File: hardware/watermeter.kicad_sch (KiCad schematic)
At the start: 23 parts, among them J1 flow_meter, J2 t_in, J3 t_out, J4 USB-TYPE-C-31-M-12, SW1 Reboot, U2 ESP32-C6-MINI-1, U3 USBLC6-2SC6

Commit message: Refactoring
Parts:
- removed J2: t_in, Connector_PinHeader_2.00mm:PinHeader_1x03_P2.00mm_Horizontal, symbol Connector_Generic:Conn_01x03
- removed J3: t_out, Connector_PinHeader_2.00mm:PinHeader_1x03_P2.00mm_Horizontal, symbol Connector_Generic:Conn_01x03
- removed J4: USB-TYPE-C-31-M-12, MyFootprints:USB-HRO_TYPE-C-31-M-12, symbol MyParts:USB-TYPE-C-31-M-12
- removed R1, R2: 3.3k, Resistor_SMD:R_0805_2012Metric, symbol Device:R
- removed R6, R7: 22R, Resistor_SMD:R_0805_2012Metric, symbol Device:R
- removed R8, R9: 5.1, Resistor_SMD:R_0805_2012Metric, symbol Device:R
- removed U3: USBLC6-2SC6, Package_TO_SOT_SMD:SOT-23-6, symbol Power_Protection:USBLC6-2SC6
- added J1: TC2030, Connector:Tag-Connect_TC2030-IDC-NL_2x03_P1.27mm_Vertical, symbol Connector:TC2030
- added J2: EXT, Connector_PinHeader_2.54mm:PinHeader_1x13_P2.54mm_Vertical, symbol Connector:Conn_01x13_Pin
- added J4: PT1000-1, Connector_Wire:SolderWire-0.1sqmm_1x02_P3.6mm_D0.4mm_OD1mm_Relief, symbol Connector:Conn_01x02_Pin
- added J5: PT1000-2, Connector_Wire:SolderWire-0.1sqmm_1x02_P3.6mm_D0.4mm_OD1mm_Relief, symbol Connector:Conn_01x02_Pin
- C1: DIGIKEY Part # (none) -> 1276-1076-1-ND; MP (none) -> CL05A105KP5NNNC
- C2: renamed from C9; DIGIKEY Part # (none) -> 1276-1193-1-ND; MP (none) -> CL10A226MQ8NRNC
- C3: renamed from C10; DIGIKEY Part # (none) -> 311-1701-1-ND; MP (none) -> CC0402KRX7R5BB104
- D1: renamed from D26; LCSC Part # (none) -> C2297
- D2: renamed from D1; LCSC Part # (none) -> C2293
- J3: renamed from J1; footprint Connector_PinHeader_2.00mm:PinHeader_1x03_P2.00mm_Horizontal -> Connector_Wire:SolderWire-0.1sqmm_1x03_P3.6mm_D0.4mm_OD1mm_Relief
- R1: renamed from R23; LCSC Part # C25804 -> C17414
- R2: renamed from R45; LCSC Part # (none) -> C17544
- R3: renamed from R5; LCSC Part # (none) -> C17480
- R6: renamed from R3; LCSC Part # (none) -> C17513
- R7: renamed from R4; LCSC Part # (none) -> C17604
- renumbered U2 to U1
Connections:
- net +3.3V: now also J2.1 (Pin_1)
- net +5V: now also J2.12 (Pin_12)
- net 5V_USB: now also J1.2
- net GND: now also J1.4, J2.13 (Pin_13)
- net at U1.10 (IO5): now also J2.7 (Pin_7)
- net at U1.12 (IO0): now also J2.2 (Pin_2)
- net at U1.13 (IO1): now also J2.3 (Pin_3)
- net at U1.15 (IO6): now also J2.8 (Pin_8)
- net at U1.16 (IO7): now also J2.9 (Pin_9)
- net at U1.22 (IO8): now also J2.10 (Pin_10)
- net at U1.23 (IO9): now also J2.11 (Pin_11)
- net RXD: now reaches U1.30 (RXD0)
- net RXD: now also J1.5
- net TXD: now reaches U1.31 (TXD0)
- net TXD: now also J1.3
- net at U1.5 (IO2): now also J2.4 (Pin_4)
- net at U1.6 (IO3): now also J2.5 (Pin_5)
- net at U1.9 (IO4): now also J2.6 (Pin_6)
- net USB_D_N: no longer names the net of U1.17 (IO12)
- net USB_D_P: no longer names the net of U1.18 (IO13)
- new net BOOT: J1.6
- new net EN: J1.1
- no-connect marks 18 -> 3
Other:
- moved on the sheet: J3, R6, R7, U1

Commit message: Schematics done
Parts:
- removed J1: TC2030, Connector:Tag-Connect_TC2030-IDC-NL_2x03_P1.27mm_Vertical, symbol Connector:TC2030
- removed J2: EXT, Connector_PinHeader_2.54mm:PinHeader_1x13_P2.54mm_Vertical, symbol Connector:Conn_01x13_Pin
- added C10, C11, C12, C13: 0.1uF, Capacitor_SMD:C_0402_1005Metric, symbol Device:C
- added D7, D8: 1N4148W, PCM_Diode_SMD_AKL:D_SOD-123, symbol PCM_Diode_AKL:1N4148W
- added J1: NTC1, Connector_Wire:SolderWire-0.1sqmm_1x02_P3.6mm_D0.4mm_OD1mm_Relief, symbol Connector:Conn_01x02_Pin
- added J10, J11: Screw_Terminal_01x03, symbol Connector:Screw_Terminal_01x03
- added J12: Screw, symbol Connector:Screw_Terminal_01x02
- added J13, J14: Conn_01x06_Shielded, symbol Connector:Conn_01x06_Pin
- added J2: DHT21, Connector_Wire:SolderWire-0.1sqmm_1x03_P3.6mm_D0.4mm_OD1mm_Relief, symbol Connector_Generic:Conn_01x03
- added J7: NTC3, Connector_Wire:SolderWire-0.1sqmm_1x02_P3.6mm_D0.4mm_OD1mm_Relief, symbol Connector:Conn_01x02_Pin
- added J8: NTC4, Connector_Wire:SolderWire-0.1sqmm_1x02_P3.6mm_D0.4mm_OD1mm_Relief, symbol Connector:Conn_01x02_Pin
- added J9: USB-TYPE-C-31-M-12, MyFootprints:USB-HRO_TYPE-C-31-M-12, symbol MyParts:USB-TYPE-C-31-M-12
- added K1, K2: SRD-05VDC-SL-C, Relay_THT:Relay_SPDT_SANYOU_SRD_Series_Form_C, symbol Relay:SANYOU_SRD_Form_C
- added OC1, OC2: TLP2361, PCM_Package_SO_AKL:SO-5_4.4x3.6mm_P1.27mm, symbol PCM_Optocoupler_Logic_AKL:TLP2361
- added Q1, Q2: NPN, symbol Simulation_SPICE:NPN
- added R10: 10K, Resistor_SMD:R_0805_2012Metric, symbol Device:R
- added R11, R12: 5.1, Resistor_SMD:R_0805_2012Metric, symbol Device:R
- added R13, R16: 22R, Resistor_SMD:R_0805_2012Metric, symbol Device:R
- added R17, R18, R4, R5, R8, R9: 4k7, symbol Device:R
- added R19: 1k, Resistor_SMD:R_0805_2012Metric, symbol Device:R
- added U2: USBLC6-2SC6, Package_TO_SOT_SMD:SOT-23-6, symbol Power_Protection:USBLC6-2SC6
- J4: value PT1000-1 -> NTC1
- J5: value PT1000-2 -> NTC2
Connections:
- net +3.3V: now also J14.1 (Pin_1), J2.1 (Pin_1), OC2.6 (VCC), R10.1, R18.1, R4.1, R5.1, R8.1, R9.1
- net +5V: now also D7.1 (K), D8.1 (K), J13.1 (Pin_1), K1.2, K2.2, OC1.6 (VCC), R17.1
- net 5V_USB: now also J9.A4_B9 (VBUS), J9.B4_A9 (VBUS), U2.5 (VBUS)
- net GND: now also J4.2 (Pin_2), J5.2 (Pin_2), C10.2, C11.2, C12.2, C13.2, J13.6 (Pin_6), J14.6 (Pin_6), J2.3 (Pin_3), J7.2 (Pin_2), J8.2 (Pin_2), J9.A1_B12 (GND), J9.B1_A12 (GND), OC1.3, OC2.4 (GND), Q1.3 (E), Q2.3 (E), R11.2, R12.2, U2.2 (GND)
- net IO1: now reaches J4.1 (Pin_1)
- net IO1: now also U1.13 (IO1), C10.1, R9.2
- net IO23: now reaches D1.2 (A), U1.29 (IO23)
- net IO7: now reaches R6.2, R7.1
- net IO7: now also U1.16 (IO7); no longer U1.27 (IO21)
- net IO22: now reaches D2.2 (A), U1.28 (IO22)
- net IO22: now also J14.5 (Pin_5)
- net IO3: now reaches J5.1 (Pin_1)
- net IO3: now also U1.6 (IO3), C11.1, R8.2
- net IO5: now reaches U1.10 (IO5)
- net IO5: now also C13.1, J8.1 (Pin_1), R4.2
- net IO0: now reaches U1.12 (IO0)
- net IO0: now also J13.2 (Pin_2)
- net IO6: now reaches U1.15 (IO6)
- net IO6: now also J2.2 (Pin_2), R10.2
- net USB_D_N: now reaches U1.17 (IO12)
- net USB_D_N: now also R13.2
- net USB_D_P: now reaches U1.18 (IO13)
- net USB_D_P: now also R16.2
- net IO14: now reaches U1.19 (IO14)
- net IO14: now also OC2.5, R18.2
- net IO15: now reaches U1.20 (IO15)
- net IO15: now also OC1.1
- net IO8: now reaches U1.22 (IO8)
- net IO8: now also J13.4 (Pin_4)
- net IO9: now reaches U1.23 (IO9)
- net IO9: now also J13.5 (Pin_5)
- net IO18: now reaches U1.24 (IO18)
- net IO18: now also Q1.2 (B)
- net IO19: now reaches U1.25 (IO19)
- net IO19: now also Q2.2 (B)
- net IO20: now reaches U1.26 (IO20)
- net IO2: now reaches U1.5 (IO2)
- net IO2: now also J13.3 (Pin_3)
- net IO4: now reaches U1.9 (IO4)
- net IO4: now also C12.1, J7.1 (Pin_1), R5.2
- net RXD renamed RXD0
- net RXD0: now also J14.3 (Pin_3)
- net TXD renamed TXD0
- net TXD0: now also J14.2 (Pin_2)
- new net: R13.1, U2.6 (I/O1)
- new net: D8.2 (A), K2.5, Q2.1 (C)
- new net: J9.B5 (CC2), R12.1
- new net: J1.1 (Pin_1), R19.1
- new net: OC2.1, R19.2
- new net: D7.2 (A), K1.5, Q1.1 (C)
- new net: R16.1, U2.4 (I/O2)
- new net: J9.A5 (CC1), R11.1
- new net: J12.1 (Pin_1), OC1.5, R17.2
- new net: J9.S1 (SHIELD), J9.S2 (SHIELD), J9.S3 (SHIELD), J9.S4 (SHIELD)
- new net COM1: J10.2 (Pin_2), K1.1
- new net COM2: J11.2 (Pin_2), K2.1
- new net D+: J9.A6 (DP1), J9.B6 (DP2), U2.3 (I/O2)
- new net D-: J9.A7 (DN1), J9.B7 (DN2), U2.1 (I/O1)
- new net GND1: J1.2 (Pin_2), J12.2 (Pin_2), OC1.4 (GND), OC2.3
- new net IO21: J14.4 (Pin_4), U1.27 (IO21)
- new net NC1: J10.3 (Pin_3), K1.4
- new net NC2: J11.3 (Pin_3), K2.4
- new net NO1: J10.1 (Pin_1), K1.3
- new net NO2: J11.1 (Pin_1), K2.3
- no-connect marks 3 -> 4
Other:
- note added: "DHT21/DS18B20"
- note added: "HALL flow sensor"
- note added: "NTC inputs"
- note added: "PWM in"
- note added: "PWM out"
- note added: "Relay1"
- note added: "Relay2"
- moved on the sheet: D1, D2, J3, J4, J5, R2, R3, R6, R7

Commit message: Release hardware design v1.0 for manufacturing
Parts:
- removed J12: Screw, symbol Connector:Screw_Terminal_01x02
- removed J4: NTC1, Connector_Wire:SolderWire-0.1sqmm_1x02_P3.6mm_D0.4mm_OD1mm_Relief, symbol Connector:Conn_01x02_Pin
- removed J5: NTC2, Connector_Wire:SolderWire-0.1sqmm_1x02_P3.6mm_D0.4mm_OD1mm_Relief, symbol Connector:Conn_01x02_Pin
- removed J8: NTC4, Connector_Wire:SolderWire-0.1sqmm_1x02_P3.6mm_D0.4mm_OD1mm_Relief, symbol Connector:Conn_01x02_Pin
- added H1, H2, H3, H4: MountingHole, MountingHole:MountingHole_3.2mm_M3_ISO7380, symbol Mechanical:MountingHole
- added J3: Conn_01x08_Pin, TerminalBlock_Phoenix:TerminalBlock_Phoenix_MKDS-1,5-8-5.08_1x08_P5.08mm_Horizontal, symbol Connector:Conn_01x08_Pin
- J1: renamed from J10; footprint (none) -> TerminalBlock_Phoenix:TerminalBlock_Phoenix_MKDS-1,5-3-5.08_1x03_P5.08mm_Horizontal; LCSC Part # (none) -> C2915640
- J10: renamed from J3; footprint Connector_Wire:SolderWire-0.1sqmm_1x03_P3.6mm_D0.4mm_OD1mm_Relief -> TerminalBlock_Phoenix:TerminalBlock_Phoenix_MKDS-1,5-3-5.08_1x03_P5.08mm_Horizontal; LCSC Part # (none) -> C2915640; now fitted; now in the parts list
- J11: renamed from J9; LCSC Part # (none) -> C165948
- J2: renamed from J11; footprint (none) -> TerminalBlock_Phoenix:TerminalBlock_Phoenix_MKDS-1,5-3-5.08_1x03_P5.08mm_Horizontal; LCSC Part # (none) -> C2915640
- J4: renamed from J13; footprint (none) -> Connector_PinHeader_2.54mm:PinHeader_1x06_P2.54mm_Vertical; now not fitted; now left out of the parts list
- J6: renamed from J1; value NTC1 -> PWM_IN; footprint Connector_Wire:SolderWire-0.1sqmm_1x02_P3.6mm_D0.4mm_OD1mm_Relief -> TerminalBlock_Phoenix:TerminalBlock_Phoenix_MKDS-1,5-2-5.08_1x02_P5.08mm_Horizontal; LCSC Part # (none) -> C2915639; now fitted; now in the parts list
- J7: value NTC3 -> PWM_OUT; footprint Connector_Wire:SolderWire-0.1sqmm_1x02_P3.6mm_D0.4mm_OD1mm_Relief -> TerminalBlock_Phoenix:TerminalBlock_Phoenix_MKDS-1,5-2-5.08_1x02_P5.08mm_Horizontal; LCSC Part # (none) -> C2915639; now fitted; now in the parts list
- J8: renamed from J2; footprint Connector_Wire:SolderWire-0.1sqmm_1x03_P3.6mm_D0.4mm_OD1mm_Relief -> TerminalBlock_Phoenix:TerminalBlock_Phoenix_MKDS-1,5-3-5.08_1x03_P5.08mm_Horizontal; LCSC Part # (none) -> C2915640; now fitted; now in the parts list
- J9: renamed from J14; footprint (none) -> Connector_PinHeader_2.54mm:PinHeader_1x06_P2.54mm_Vertical; now not fitted; now left out of the parts list
- K1, K2: LCSC Part # (none) -> C35449
- OC1, OC2: LCSC Part # (none) -> C107626
- Q1, Q2: footprint (none) -> PCM_Package_TO_SOT_SMD_AKL:SOT-23; LCSC Part # (none) -> C150982
- R10: renamed from R5; footprint (none) -> Resistor_SMD:R_0805_2012Metric; LCSC Part # (none) -> C17673
- R11: renamed from R12; value 5.1 -> 5k1; LCSC Part # (none) -> C27834
- R12: renamed from R11; value 5.1 -> 5k1; LCSC Part # (none) -> C27834
- R13: LCSC Part # (none) -> C17561
- R14: renamed from R16; LCSC Part # (none) -> C17561
- R5: renamed from R18; footprint (none) -> Resistor_SMD:R_0805_2012Metric; LCSC Part # (none) -> C17673
- R6: renamed from R4; footprint (none) -> Resistor_SMD:R_0805_2012Metric; LCSC Part # (none) -> C17673
- R7: renamed from R8; footprint (none) -> Resistor_SMD:R_0805_2012Metric; LCSC Part # (none) -> C17673
- R8: renamed from R9; footprint (none) -> Resistor_SMD:R_0805_2012Metric; LCSC Part # (none) -> C17673
- R9: renamed from R17; footprint (none) -> Resistor_SMD:R_0805_2012Metric; LCSC Part # (none) -> C17673
- renumbered C11 to C1, C10 to C2, C12 to C3, C13 to C4, C1 to C6, C2 to C7, C3 to C8, D7 to D1, D8 to D2, D2 to D3, D1 to D4, R10 to R15, R7 to R18, R6 to R19, R3 to R2, R2 to R3, R19 to R4
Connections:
- net GND1 is gone; now on net GND: J6.2 (Pin_2), OC1.4 (GND), OC2.3
- net GND: now also J3.2 (Pin_2), J3.4 (Pin_4), J3.6 (Pin_6), J3.8 (Pin_8)
- net IO1: now also J3.1 (Pin_1)
- net IO3: now also J3.3 (Pin_3)
- net IO4: now also J3.5 (Pin_5); no longer J7.1 (Pin_1)
- net IO5: now also J3.7 (Pin_7)
- net at OC1.5, R9.2: now also J7.1 (Pin_1)
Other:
- note added: "External connector"
- moved on the sheet: D1, D2, J1, J11, J2, K1, K2, OC2, Q1, Q2, R11, R12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

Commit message: fix: unstable power supply
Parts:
- removed C7: 22uF, Capacitor_SMD:C_0603_1608Metric, symbol Device:C
- added C14: 47uF/16V, Capacitor_SMD:C_1210_3225Metric, symbol Device:C
- added C7: 10uF/10V, Capacitor_SMD:C_1206_3216Metric, symbol PCM_Capacitor_AKL:C_0805
- C8: value 0.1uF -> 0.1uF/6.3v; footprint Capacitor_SMD:C_0402_1005Metric -> Capacitor_SMD:C_0805_2012Metric; LCSC Part # C541406 -> C1854118
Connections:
- net +3.3V: now also C14.1, C7.1
- net GND: now also C14.2, C7.2
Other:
- note added: "ToDo: Опроводяване наново с 1мм писти за 3.3v и 5V Евентуално смяна на стабилизатора за 3.3V Подпиране с електролитни или танталови кондензатори на Dc-Dc и модул"

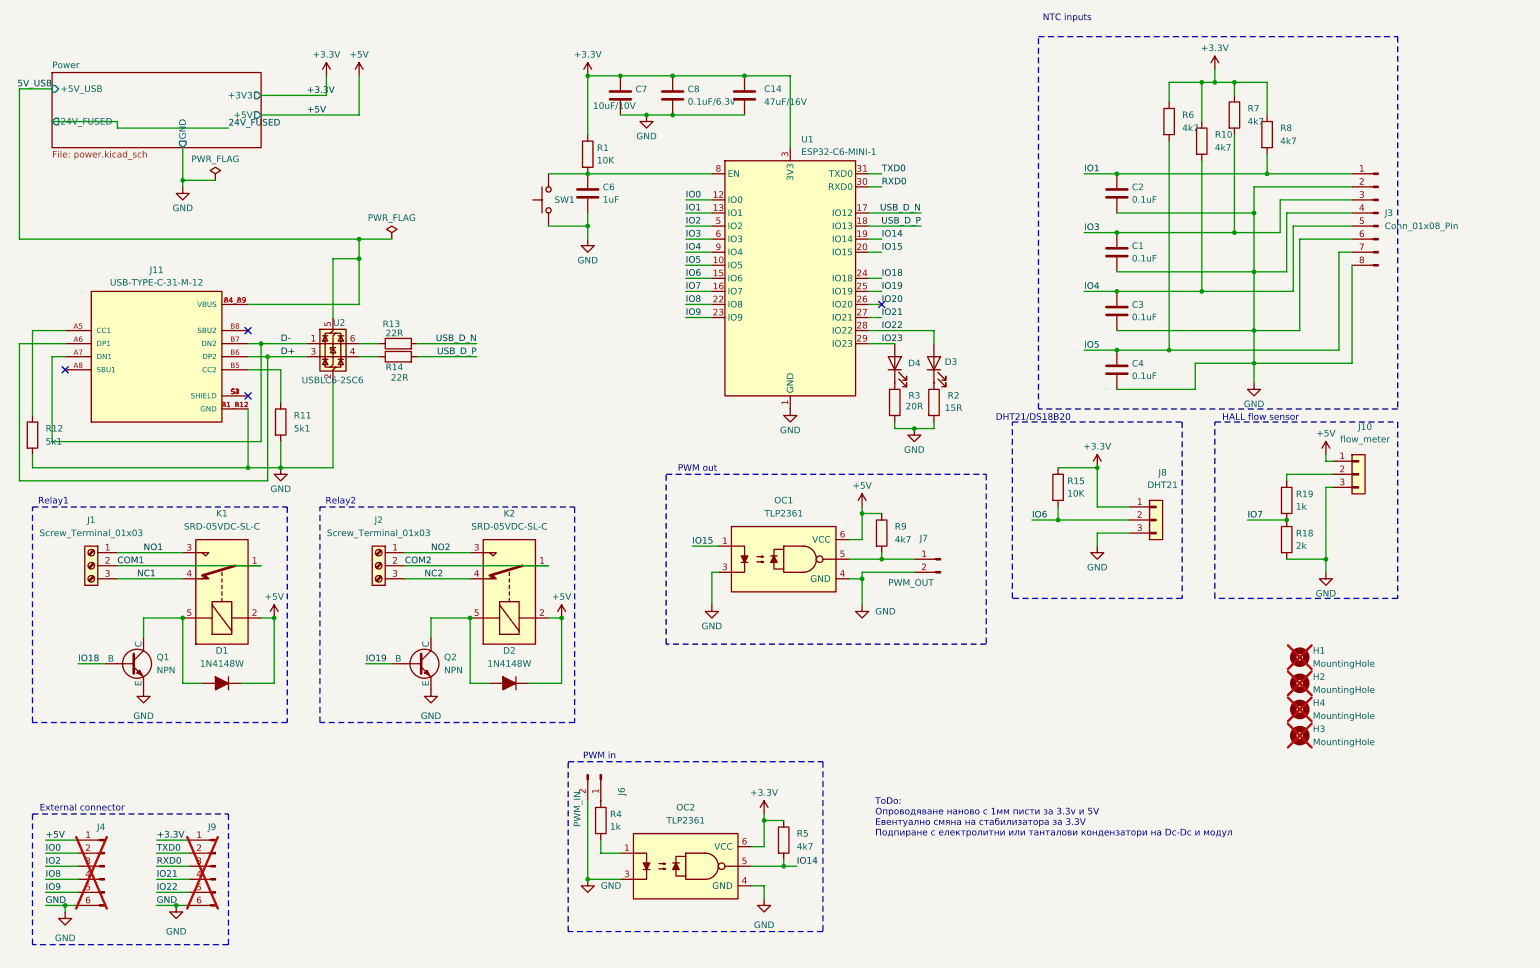
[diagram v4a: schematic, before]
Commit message: Board V2. fix: power supply fix: NTC noise suppression fix: Q1 and Q2 wrong pin numbers fix: Increased power trice width
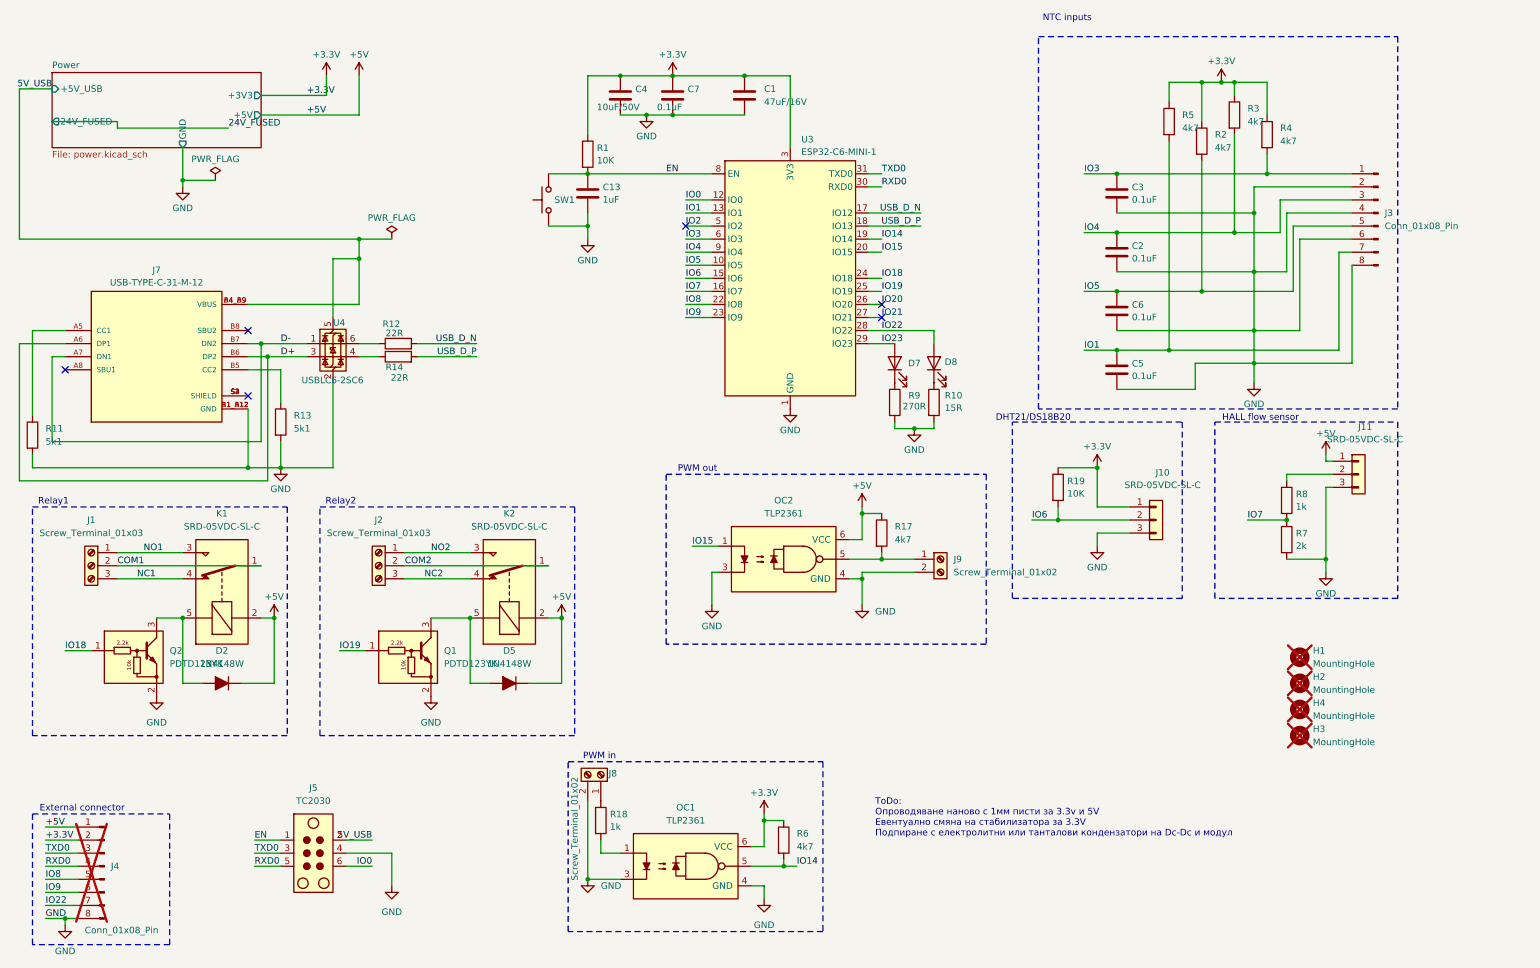
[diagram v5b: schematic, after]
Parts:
- removed C7: 10uF/10V, Capacitor_SMD:C_1206_3216Metric, symbol PCM_Capacitor_AKL:C_0805
- removed J4, J9: Conn_01x06_Shielded, Connector_PinHeader_2.54mm:PinHeader_1x06_P2.54mm_Vertical, symbol Connector:Conn_01x06_Pin
- removed J6: PWM_IN, TerminalBlock_Phoenix:TerminalBlock_Phoenix_MKDS-1,5-2-5.08_1x02_P5.08mm_Horizontal, symbol Connector:Conn_01x02_Pin
- removed J7: PWM_OUT, TerminalBlock_Phoenix:TerminalBlock_Phoenix_MKDS-1,5-2-5.08_1x02_P5.08mm_Horizontal, symbol Connector:Conn_01x02_Pin
- removed Q1, Q2: NPN, PCM_Package_TO_SOT_SMD_AKL:SOT-23, symbol Simulation_SPICE:NPN
- added C4: 10uF/50V, Capacitor_SMD:C_1206_3216Metric, symbol Device:C
- added J4: Conn_01x08_Pin, Connector_PinHeader_2.54mm:PinHeader_1x08_P2.54mm_Vertical, symbol Connector:Conn_01x08_Pin
- added J5: TC2030, Connector:Tag-Connect_TC2030-IDC-NL_2x03_P1.27mm_Vertical, symbol Connector:TC2030
- added J8, J9: Screw_Terminal_01x02, TerminalBlock_Phoenix:TerminalBlock_Phoenix_MKDS-1,5-2-5.08_1x02_P5.08mm_Horizontal, symbol Connector:Screw_Terminal_01x02
- added Q1, Q2: PDTD123YK, PCM_Package_TO_SOT_SMD_AKL:SC-59, symbol PCM_Transistor_BJT_Pre-Biased_AKL:PDTD123YK
- C1: renamed from C14; footprint Capacitor_SMD:C_1210_3225Metric -> Capacitor_SMD:C_1206_3216Metric; LCSC Part # C5189825 -> C96123
- C2: renamed from C1; footprint Capacitor_SMD:C_0402_1005Metric -> Capacitor_SMD:C_1206_3216Metric; LCSC Part # C541406 -> C24497
- C3: renamed from C2; footprint Capacitor_SMD:C_0402_1005Metric -> Capacitor_SMD:C_1206_3216Metric; LCSC Part # C541406 -> C24497
- C5: renamed from C4; footprint Capacitor_SMD:C_0402_1005Metric -> Capacitor_SMD:C_1206_3216Metric; LCSC Part # C541406 -> C24497
- C6: renamed from C3; footprint Capacitor_SMD:C_0402_1005Metric -> Capacitor_SMD:C_1206_3216Metric; LCSC Part # C541406 -> C24497
- C7: renamed from C8; value 0.1uF/6.3v -> 0.1uF; footprint Capacitor_SMD:C_0805_2012Metric -> Capacitor_SMD:C_1206_3216Metric; LCSC Part # C1854118 -> C24497
- D2: renamed from D1; footprint PCM_Diode_SMD_AKL:D_SOD-123 -> Diode_SMD:D_SOD-323_HandSoldering; LCSC Part # (none) -> C2128
- D5: renamed from D2; footprint PCM_Diode_SMD_AKL:D_SOD-123 -> Diode_SMD:D_SOD-323_HandSoldering; LCSC Part # (none) -> C2128
- J10: renamed from J8; value DHT21 -> SRD-05VDC-SL-C
- J11: renamed from J10; value flow_meter -> SRD-05VDC-SL-C
- J7: renamed from J11; LCSC C165948 -> (none)
- R9: renamed from R3; value 20R -> 270R; footprint Resistor_SMD:R_0805_2012Metric -> Digikey library:LED_0603; LCSC Part # C17544 -> C22966
- renumbered C6 to C13, D4 to D7, D3 to D8, OC2 to OC1, OC1 to OC2, R2 to R10, R12 to R11, R13 to R12, R11 to R13, R9 to R17, R4 to R18, R15 to R19, R10 to R2, R7 to R3, R8 to R4, R6 to R5, R5 to R6, R18 to R7, R19 to R8, U1 to U3, U2 to U4
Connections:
- net +3.3V: now also C4.1, J4.2 (Pin_2)
- net +5V: now also J4.1 (Pin_1)
- net 5V_USB: now also J5.2
- net GND: now also C4.2, J4.8 (Pin_8), J5.4, J8.2 (Pin_2), J9.2 (Pin_2), Q1.2 (E), Q2.2 (E)
- net IO0: now also J5.6
- net IO1: now also C5.1, J3.7 (Pin_7), R5.2; no longer C3.1, J3.1 (Pin_1), R4.2
- net IO18: now also Q2.1 (B)
- net IO19: now also Q1.1 (B)
- net IO22: now also J4.7 (Pin_7)
- net IO3: now also C3.1, J3.1 (Pin_1), R4.2; no longer C2.1, J3.3 (Pin_3), R3.2
- net IO4: now also C2.1, J3.3 (Pin_3), R3.2; no longer C6.1, J3.5 (Pin_5), R2.2
- net IO5: now also C6.1, J3.5 (Pin_5), R2.2; no longer C5.1, J3.7 (Pin_7), R5.2
- net IO8: now also J4.5 (Pin_5)
- net IO9: now also J4.6 (Pin_6)
- net RXD0: now also J4.4 (Pin_4), J5.5
- net TXD0: now also J4.3 (Pin_3), J5.3
- net EN: now reaches C13.1, R1.2, SW1.2, U3.8 (EN)
- net EN: now also J5.1
- net at D5.2 (A), K2.5: now also Q1.3 (C)
- net at R18.1: now also J8.1 (Pin_1)
- net at D2.2 (A), K1.5: now also Q2.3 (C)
- net at OC2.5, R17.2: now also J9.1 (Pin_1)
- no-connect marks 4 -> 6
